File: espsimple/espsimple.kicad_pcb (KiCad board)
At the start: 2 copper layers, 13 parts, among them J1 Conn_01x02_Female, J2 Conn_01x08, J3 Conn_01x08, SW1 SW_Push, U1 ESP-12F, U2 AMS1117-3.3

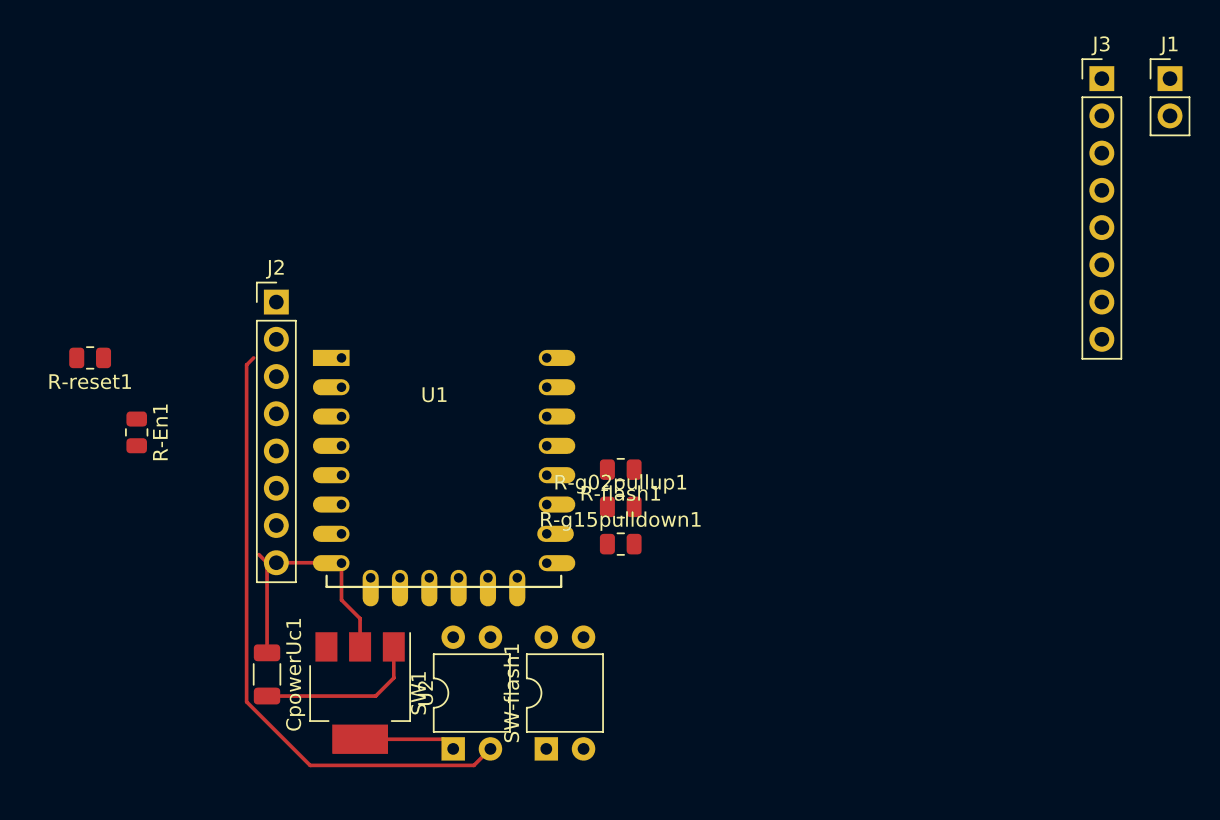
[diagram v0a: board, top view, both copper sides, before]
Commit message: finish board for esp12
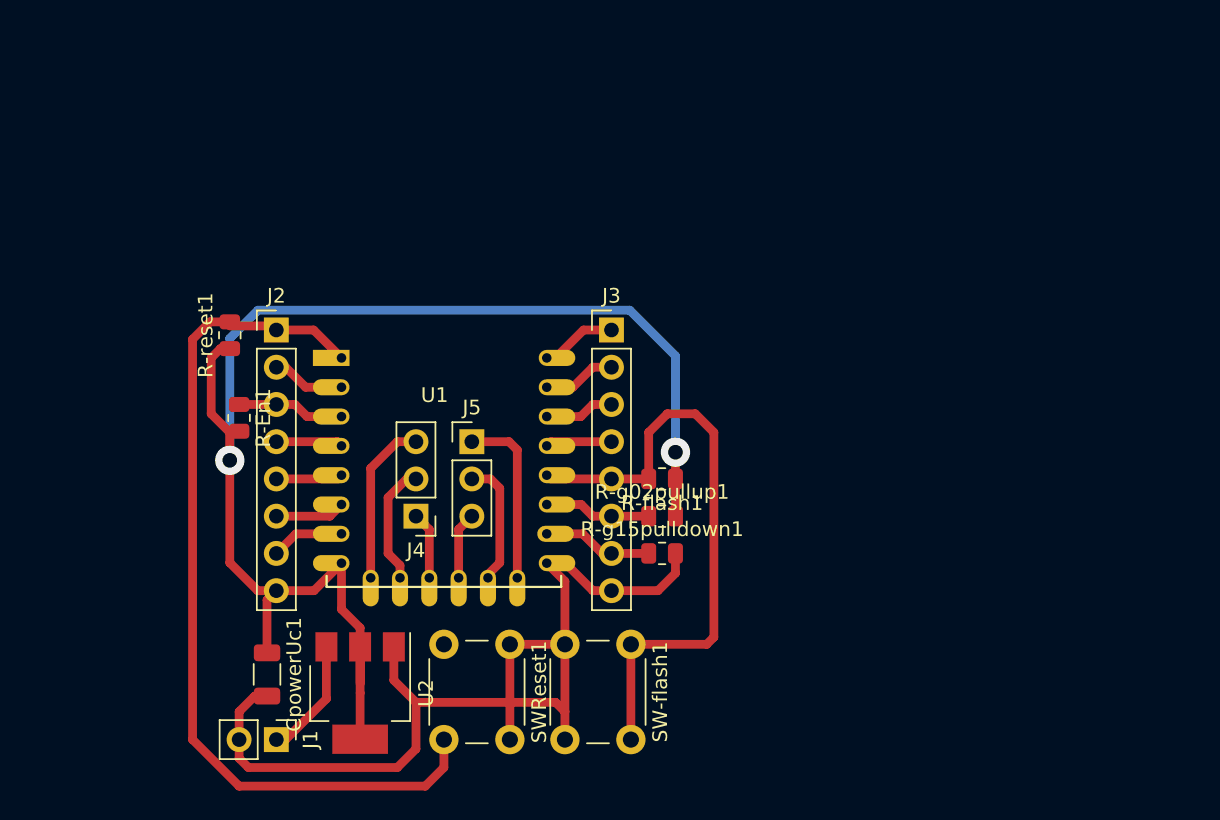
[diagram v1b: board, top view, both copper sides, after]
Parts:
- added J4: conn1x3, Connector_PinHeader_2.54mm:PinHeader_1x03_P2.54mm_Vertical, F.Cu at (151.1, 146.7)
- added J5: conn1x3, Connector_PinHeader_2.54mm:PinHeader_1x03_P2.54mm_Vertical, F.Cu at (154.9, 141.6)
- J2, J3: value Conn_01x08 -> (none)
- SW-flash1: value SW_Push -> SWflash; footprint Package_DIP:DIP-4_W7.62mm -> Button_Switch_THT:SW_PUSH_6mm
- SWReset1: renamed from SW1; value SW_Push -> SWReset; footprint Package_DIP:DIP-4_W7.62mm -> Button_Switch_THT:SW_PUSH_6mm
- moved J1 75.8 mm to (141.6, 161.9), turned to 270 degrees
- moved J3 37.6 mm to (164.5, 134.0)
- moved R-reset1 9.65 mm to (138.4, 134.3), turned to 90 degrees
- moved SW-flash1 9.18 mm to (165.8, 155.4), turned to 270 degrees
- moved SWReset1 8.11 mm to (157.5, 155.4), turned to 270 degrees
- moved R-En1 7.06 mm to (139.1, 140.0)
- moved R-flash1 2.89 mm to (167.9, 144.1)
- moved R-g02pullup1 2.89 mm to (167.9, 146.7)
- moved R-g15pulldown1 2.89 mm to (167.9, 149.2)
- moved J2 1.91 mm to (141.6, 134.0)
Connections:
- R-reset1 pad 1: Net-(J2-Pad1) -> v3.3
- R-reset1 pad 2: Net-(R-reset1-Pad2) -> Net-(J2-Pad1)
- SWReset1 pad 1: v3.3 -> GND
- SWReset1 pad 2: Net-(R-reset1-Pad2) -> Net-(J2-Pad1)
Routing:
- net v3.3: track 24.9 -> 96.5 mm, vias 0 -> 2
- net Net-(J2-Pad1): track 0.00 -> 59.8 mm
- net GND: track 11.3 -> 70.6 mm
- net Net-(R-reset1-Pad2): track 42.6 -> 0.00 mm
- net Net-(J3-Pad5): track 0.00 -> 42.1 mm
- net Net-(J5-Pad1): track 0.00 -> 12.1 mm
- net Net-(J4-Pad3): track 0.00 -> 11.3 mm
- net Net-(J5-Pad2): track 0.00 -> 8.61 mm
- net Net-(J4-Pad2): track 0.00 -> 8.24 mm
- net Net-(J1-Pad1): track 0.00 -> 8.11 mm
- net Net-(J3-Pad7): track 0.00 -> 7.51 mm
- net Net-(J2-Pad3): track 0.00 -> 7.33 mm
- net Net-(J3-Pad6): track 0.00 -> 7.28 mm
- net Net-(J3-Pad1): track 0.00 -> 5.20 mm
- net Net-(J2-Pad2): track 0.00 -> 5.01 mm
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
